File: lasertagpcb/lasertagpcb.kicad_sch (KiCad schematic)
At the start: 27 parts, among them J1 Conn_01x04_Socket, J2 Conn_01x02, J3 Conn_01x02_Socket, Q1 VN2106, U1 MCP6002-xP

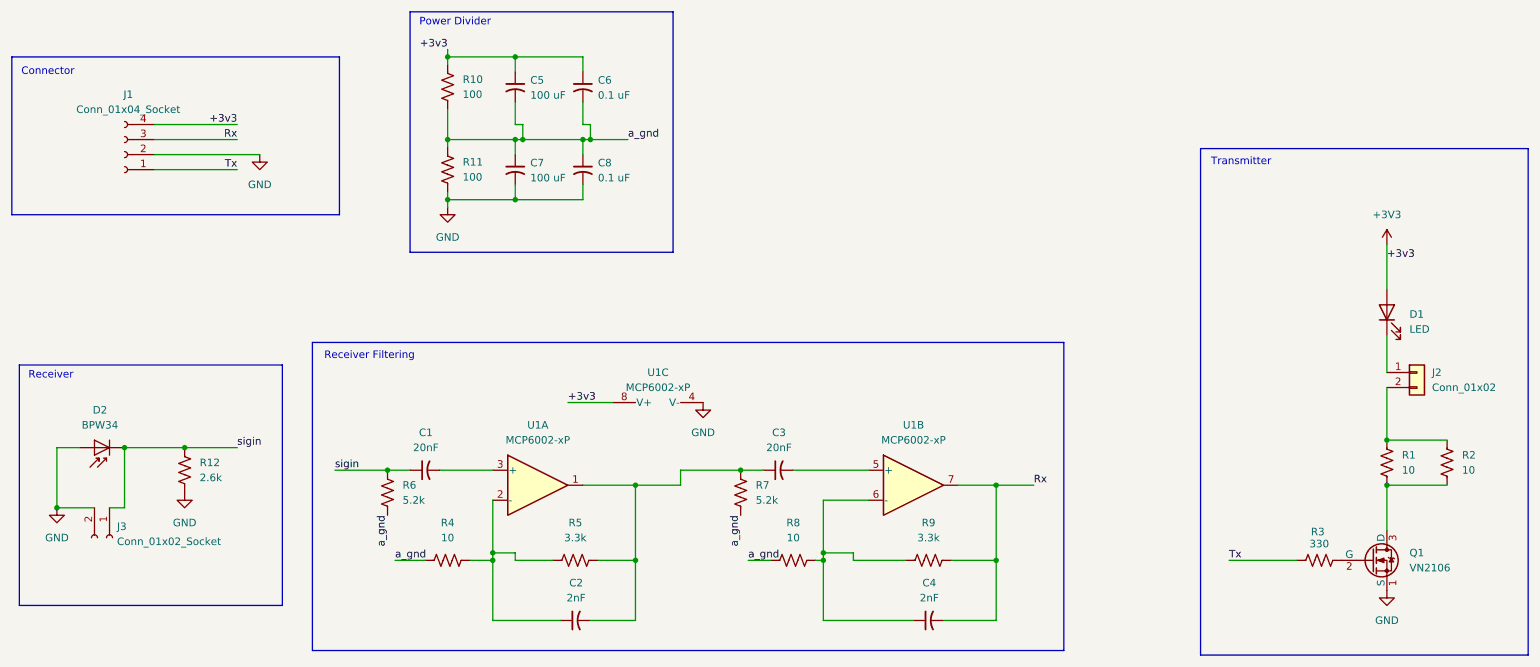
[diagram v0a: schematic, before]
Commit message: updated photo diode
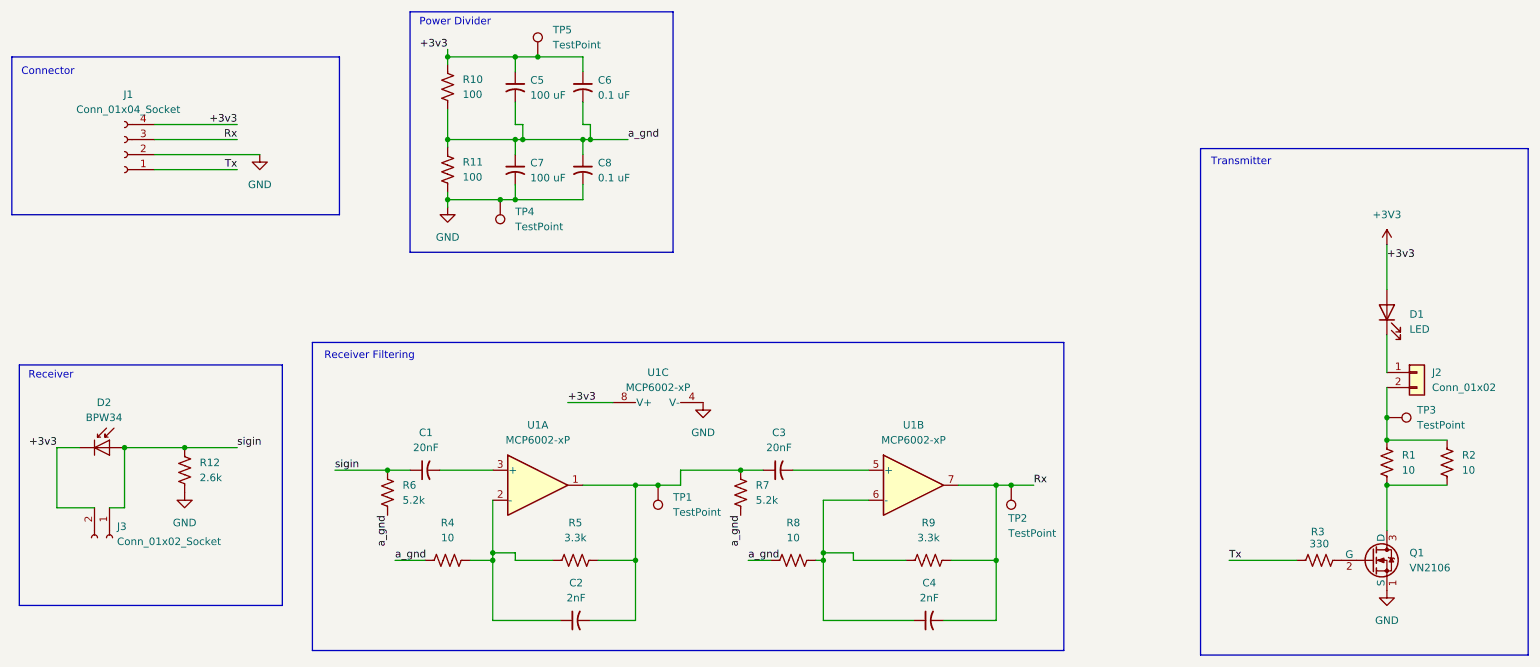
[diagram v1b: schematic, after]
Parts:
- added TP1, TP2, TP3, TP4, TP5: TestPoint, TestPoint:TestPoint_Pad_2.0x2.0mm, symbol Connector:TestPoint
- C5, C7: footprint Capacitor_THT:CP_Radial_D8.0mm_P5.00mm -> Capacitor_THT:CP_Radial_D10.0mm_P5.00mm
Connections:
- net +3V3: now also D2.1 (K), J3.2 (Pin_2), TP5.1
- net GND: now also TP4.1; no longer D2.2 (A), J3.2 (Pin_2)
- net Rx: now also TP2.1
- net sigin: now also D2.2 (A); no longer D2.1 (K)
- net at C2.2, C3.1, R5.2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: now also TP1.1
- net at J2.2 (Pin_2), R1.1, R2.1: now also TP3.1
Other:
- moved on the sheet: D2

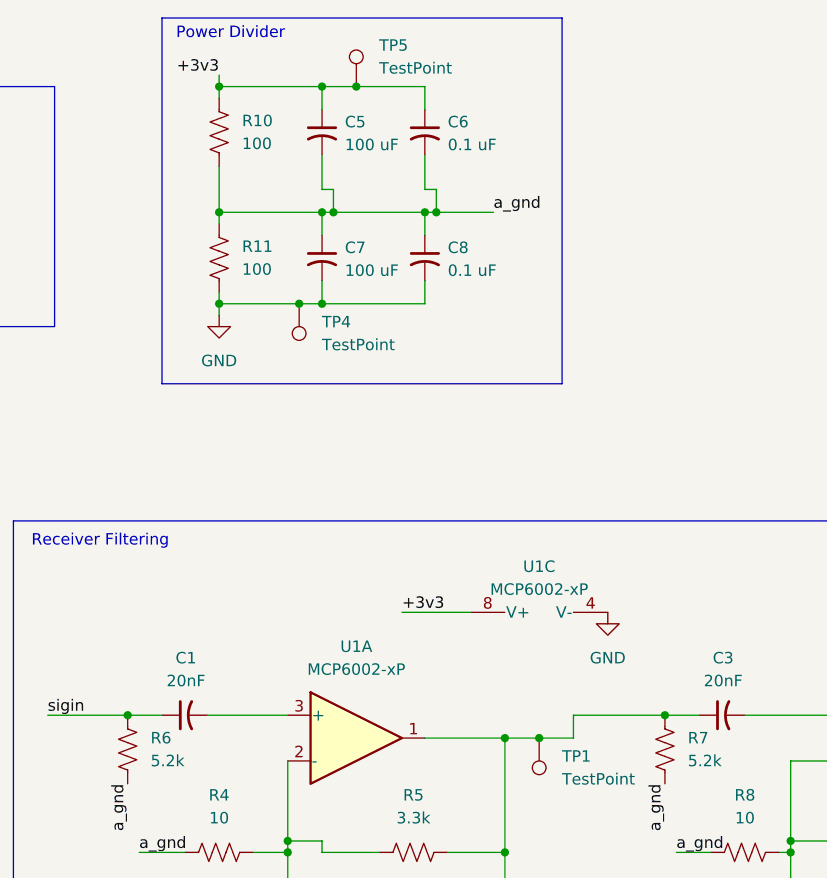
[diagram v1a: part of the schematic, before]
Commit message: Updated layout. Added decoupling caps
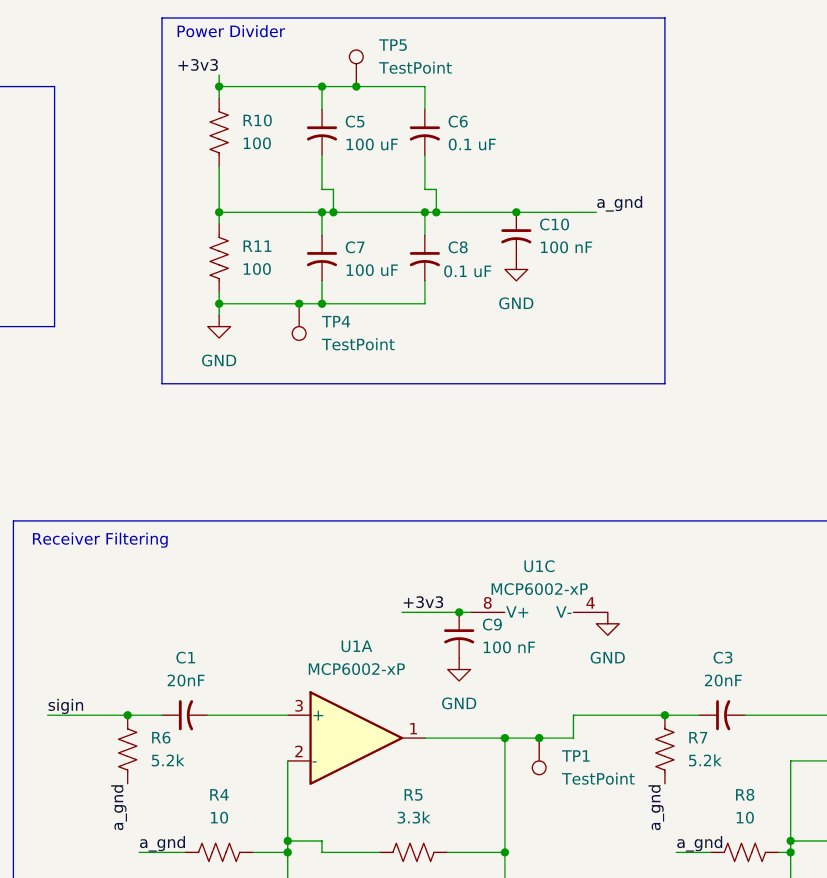
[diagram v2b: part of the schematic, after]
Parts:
- added C10, C9: 100 nF, Capacitor_SMD:C_0805_2012Metric_Pad1.18x1.45mm_HandSolder, symbol Device:C_Small_US
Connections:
- net +3V3: now also C9.1
- net GND: now also C10.2, C9.2
- net a_gnd: now also C10.1
